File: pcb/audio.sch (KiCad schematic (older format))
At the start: 40 parts, among them J1 AudioJack3_SwitchTR, U400 CS43130, U401 ADP150-3.0, U402 ADP150-1.8, U403 ADP150-1.8, U404 SN74AVC4T245PW, U405 PCA9306, X1 DSC1001CE2-022.5792

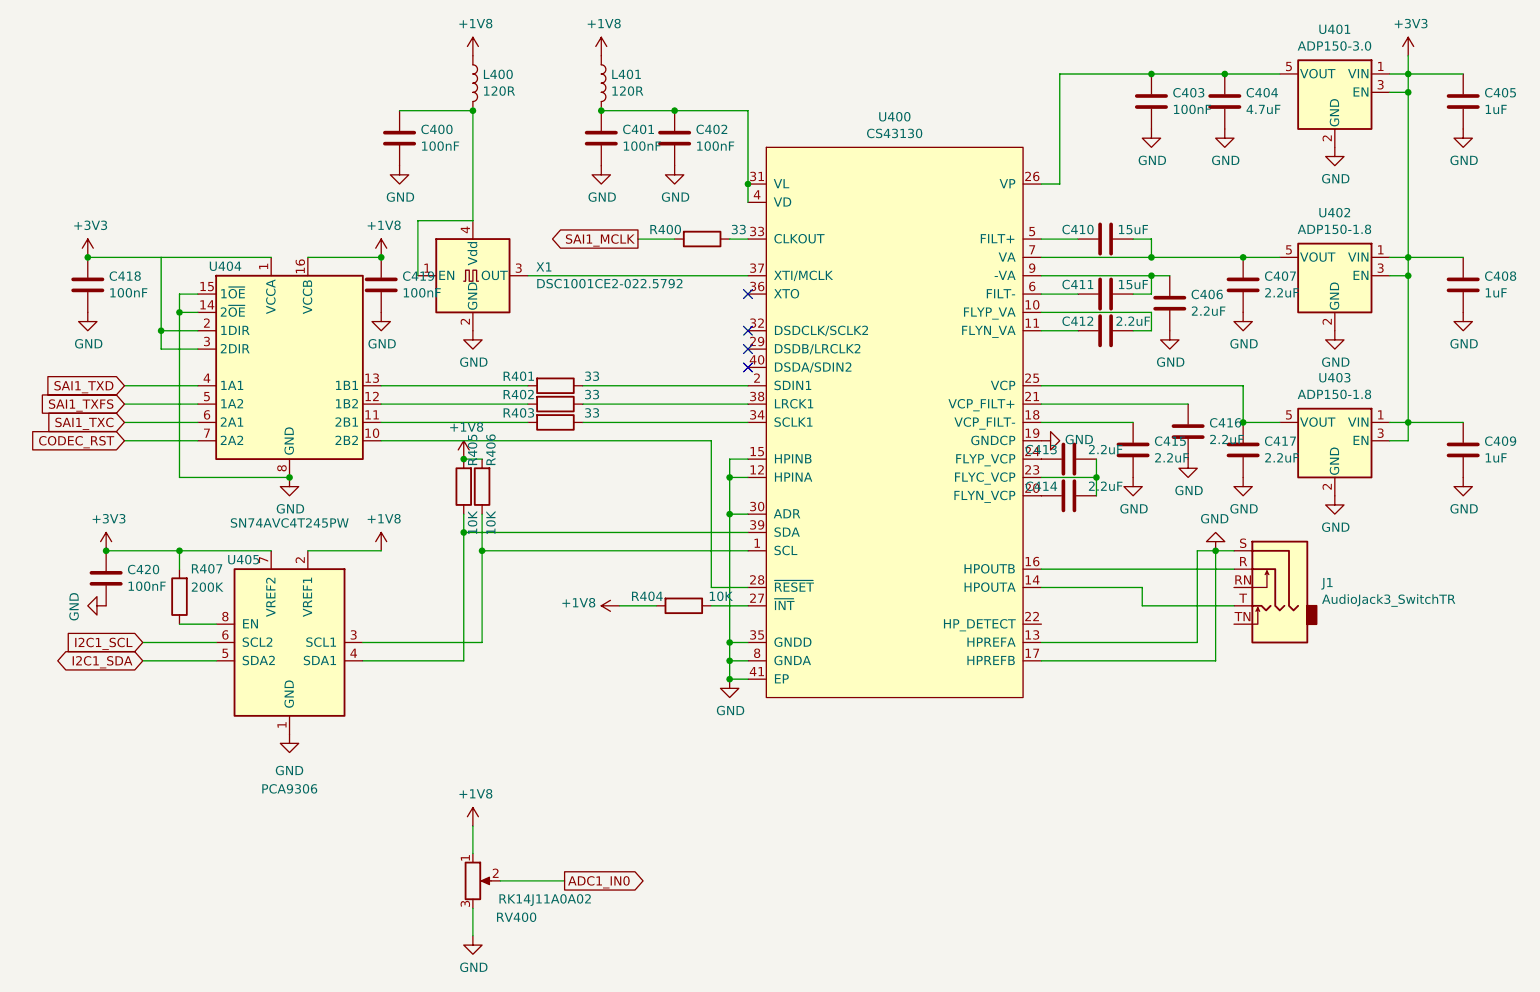
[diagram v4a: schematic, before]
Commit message: pcb: use crystal instead
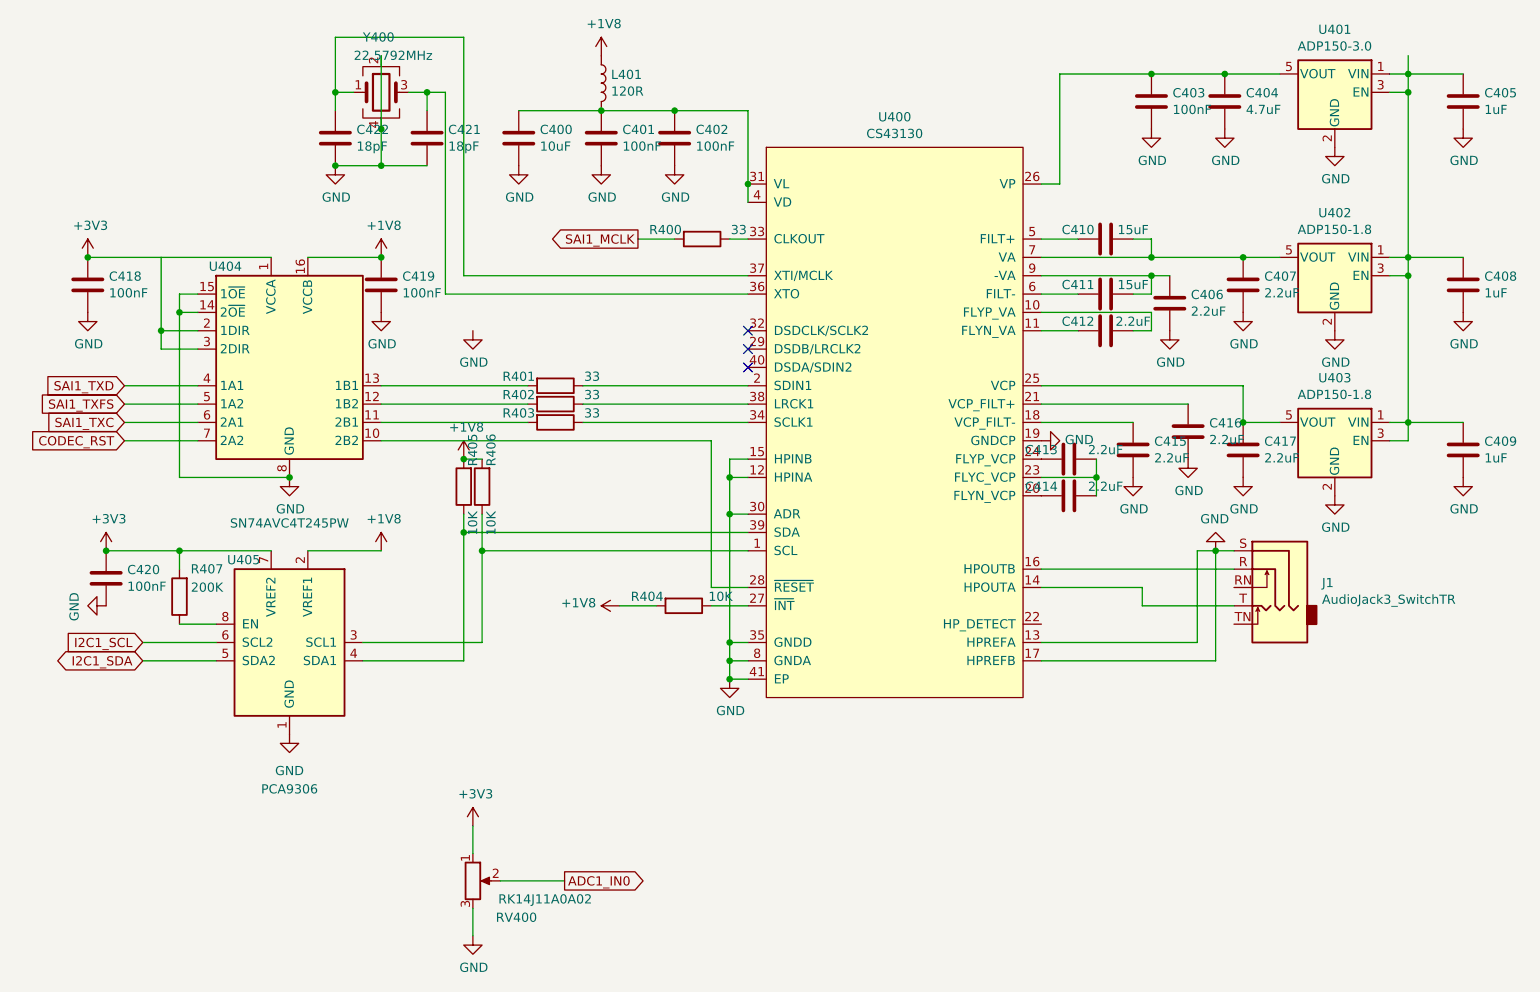
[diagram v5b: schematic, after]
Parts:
- removed L400: 120R, Inductor_SMD:L_0603_1608Metric, symbol Device:L
- removed X1: DSC1001CE2-022.5792, Oscillator:Oscillator_SMD_Abracon_ASE-4Pin_3.2x2.5mm, symbol Oscillator:ASE-xxxMHz
- added C421, C422: 18pF, Capacitor_SMD:C_0402_1005Metric, symbol Device:C
- added Y400: 22.5792MHz, Oscillator:Oscillator_SMD_Abracon_ASE-4Pin_3.2x2.5mm, symbol Device:Crystal_GND24
- C400: value 100nF -> 10uF
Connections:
- net +1V8: no longer RV400.1
- net +3V3: now also RV400.1; no longer C405.1, C408.1, C409.1, U401.1 (VIN), U401.3 (EN), U402.1 (VIN), U402.3 (EN), U403.1 (VIN), U403.3 (EN)
- net GND: now also C421.2, C422.2, Y400.2, Y400.4
- net at C401.1, C402.1, L401.2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: now also C400.1
- net at U400.36 (XTO): now also C421.1, Y400.3
- net at U400.37 (XTI/MCLK): now also C422.1, Y400.1
- new net: C405.1, C408.1, C409.1, U401.1 (VIN), U401.3 (EN), U402.1 (VIN), U402.3 (EN), U403.1 (VIN), U403.3 (EN)
- no-connect marks 4 -> 3
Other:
- moved on the sheet: C400
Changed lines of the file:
@@
 	-1   0    0    -1
-$EndComp
-$Comp
-L power:+3V3 #PWR0252
-U 1 1 5D3C5E19
-P 8600 2300
-F 0 "#PWR0252" H 8600 2150 50  0001 C CNN
-F 1 "+3V3" H 8615 2473 50  0000 C CNN
-F 2 "" H 8600 2300 50  0001 C CNN
-F 3 "" H 8600 2300 50  0001 C CNN
-	1    8600 2300
-	1    0    0    -1
 $EndComp
 Wire Wire Line
@@
 NoConn ~ 5000 3900
 NoConn ~ 5000 4000
-NoConn ~ 5000 3600
-$Comp
-L power:+1V8 #PWR0272
-U 1 1 5D485FE4
-P 3500 2300
-F 0 "#PWR0272" H 3500 2150 50  0001 C CNN
-F 1 "+1V8" H 3515 2473 50  0000 C CNN
-F 2 "" H 3500 2300 50  0001 C CNN
-F 3 "" H 3500 2300 50  0001 C CNN
-	1    3500 2300
-	1    0    0    -1
-$EndComp
 $Comp
 L Device:C C400
 U 1 1 5D487832
-P 3100 2750
-F 0 "C400" H 3215 2796 50  0000 L CNN
-F 1 "100nF" H 3215 2705 50  0000 L CNN
-F 2 "Capacitor_SMD:C_0402_1005Metric" H 3138 2600 50  0001 C CNN
-F 3 "~" H 3100 2750 50  0001 C CNN
-	1    3100 2750
+P 3750 2750
+F 0 "C400" H 3865 2796 50  0000 L CNN
+F 1 "10uF" H 3865 2705 50  0000 L CNN
+F 2 "Capacitor_SMD:C_0402_1005Metric" H 3788 2600 50  0001 C CNN
+F 3 "~" H 3750 2750 50  0001 C CNN
+	1    3750 2750
 	1    0    0    -1
 $EndComp
@@
 L power:GND #PWR0273
 U 1 1 5D487838
-P 3100 2900
-F 0 "#PWR0273" H 3100 2650 50  0001 C CNN
-F 1 "GND" H 3105 2727 50  0000 C CNN
-F 2 "" H 3100 2900 50  0001 C CNN
-F 3 "" H 3100 2900 50  0001 C CNN
-	1    3100 2900
-	1    0    0    -1
-$EndComp
-Wire Wire Line
-	3100 2600 3500 2600
-Wire Wire Line
-	3500 3200 3500 2600
-Connection ~ 3500 2600
+P 3750 2900
+F 0 "#PWR0273" H 3750 2650 50  0001 C CNN
+F 1 "GND" H 3755 2727 50  0000 C CNN
+F 2 "" H 3750 2900 50  0001 C CNN
+F 3 "" H 3750 2900 50  0001 C CNN
+	1    3750 2900
+	1    0    0    -1
+$EndComp
 $Comp
 L power:GND #PWR0274
@@
 	1    0    0    -1
 $EndComp
-Wire Wire Line
-	3200 3500 3200 3200
-Wire Wire Line
-	3200 3200 3500 3200
-Wire Wire Line
-	3800 3500 5000 3500
 $Comp
 L Device:L L401
@@
 F 3 "~" H 4200 2450 50  0001 C CNN
 	1    4200 2450
-	1    0    0    -1
-$EndComp
-$Comp
-L Device:L L400
-U 1 1 5D4999E2
-P 3500 2450
-F 0 "L400" H 3553 2496 50  0000 L CNN
-F 1 "120R" H 3553 2405 50  0000 L CNN
-F 2 "Inductor_SMD:L_0603_1608Metric" H 3500 2450 50  0001 C CNN
-F 3 "~" H 3500 2450 50  0001 C CNN
-	1    3500 2450
 	1    0    0    -1
 $EndComp
@@
 Wire Wire Line
 	1600 4300 2000 4300
-$Comp
-L Oscillator:ASE-xxxMHz X1
-U 1 1 5D80F8A2
-P 3500 3500
-AR Path="/5D438133/5D80F8A2" Ref="X1"  Part="1"
-AR Path="/5DB2122B/5D80F8A2" Ref="X?"  Part="1"
-F 0 "X1" H 3844 3546 50  0000 L CNN
-F 1 "DSC1001CE2-022.5792" H 3844 3455 50  0000 L CNN
-F 2 "Oscillator:Oscillator_SMD_Abracon_ASE-4Pin_3.2x2.5mm" H 4200 3150 50  0001 C CNN
-F 3 "http://www.abracon.com/Oscillators/ASV.pdf" H 3400 3500 50  0001 C CNN
-	1    3500 3500
-	1    0    0    -1
-$EndComp
 Wire Wire Line
 	4100 4100 5000 4100
@@
 	4600 3300 4400 3300
 $Comp
-L power:+1V8 #PWR0102
-U 1 1 5D77A87B
-P 3500 6500
-F 0 "#PWR0102" H 3500 6350 50  0001 C CNN
-F 1 "+1V8" H 3515 6673 50  0000 C CNN
-F 2 "" H 3500 6500 50  0001 C CNN
-F 3 "" H 3500 6500 50  0001 C CNN
-	1    3500 6500
-	1    0    0    -1
-$EndComp
-$Comp
 L Logic_LevelTranslator:SN74AVC4T245PW U404
 U 1 1 5D8C4C20
@@
 Connection ~ 1400 3400
 $Comp
-L power:+1V8 #PWR?
+L power:+1V8 #PWR0142
 U 1 1 5DA41BB7
 P 3000 3400
-F 0 "#PWR?" H 3000 3250 50  0001 C CNN
+F 0 "#PWR0142" H 3000 3250 50  0001 C CNN
 F 1 "+1V8" H 3015 3573 50  0000 C CNN
 F 2 "" H 3000 3400 50  0001 C CNN
@@
 Connection ~ 3000 3400
 $Comp
-L power:GND #PWR?
+L power:GND #PWR0143
 U 1 1 5DA4A9B1
 P 3000 3700
-F 0 "#PWR?" H 3000 3450 50  0001 C CNN
+F 0 "#PWR0143" H 3000 3450 50  0001 C CNN
 F 1 "GND" H 3005 3527 50  0000 C CNN
 F 2 "" H 3000 3700 50  0001 C CNN
@@
 Connection ~ 1500 5000
 $Comp
-L power:GND #PWR?
+L power:GND #PWR0144
 U 1 1 5DA56209
 P 1500 5300
-F 0 "#PWR?" H 1500 5050 50  0001 C CNN
+F 0 "#PWR0144" H 1500 5050 50  0001 C CNN
 F 1 "GND" H 1505 5127 50  0000 C CNN
 F 2 "" H 1500 5300 50  0001 C CNN
@@
 	0    1    1    0
 $EndComp
+$Comp
+L power:+3V3 #PWR?
+U 1 1 5DBD75D1
+P 3500 6500
+F 0 "#PWR?" H 3500 6350 50  0001 C CNN
+F 1 "+3V3" H 3515 6673 50  0000 C CNN
+F 2 "" H 3500 6500 50  0001 C CNN
+F 3 "" H 3500 6500 50  0001 C CNN
+	1    3500 6500
+	1    0    0    -1
+$EndComp
+$Comp
+L Device:Crystal_GND24 Y?
+U 1 1 5DC89C50
+P 3000 2500
+AR Path="/5D4C99F9/5DC89C50" Ref="Y?"  Part="1"
+AR Path="/5D438133/5DC89C50" Ref="Y400"  Part="1"
+F 0 "Y400" H 2900 2800 50  0000 L CNN
+F 1 "22.5792MHz" H 2850 2700 50  0000 L CNN
+F 2 "Oscillator:Oscillator_SMD_Abracon_ASE-4Pin_3.2x2.5mm" H 3000 2500 50  0001 C CNN
+F 3 "~" H 3000 2500 50  0001 C CNN
+	1    3000 2500
+	1    0    0    -1
+$EndComp
+$Comp
+L Device:C C?
+U 1 1 5DC89C56
+P 2750 2750
+AR Path="/5D4C99F9/5DC89C56" Ref="C?"  Part="1"
+AR Path="/5D438133/5DC89C56" Ref="C422"  Part="1"
+F 0 "C422" H 2865 2796 50  0000 L CNN
+F 1 "18pF" H 2865 2705 50  0000 L CNN
+F 2 "Capacitor_SMD:C_0402_1005Metric" H 2788 2600 50  0001 C CNN
+F 3 "~" H 2750 2750 50  0001 C CNN
+	1    2750 2750
+	1    0    0    -1
+$EndComp
+$Comp
+L Device:C C?
+U 1 1 5DC89C5C
+P 3250 2750
+AR Path="/5D4C99F9/5DC89C5C" Ref="C?"  Part="1"
+AR Path="/5D438133/5DC89C5C" Ref="C421"  Part="1"
+F 0 "C421" H 3365 2796 50  0000 L CNN
+F 1 "18pF" H 3365 2705 50  0000 L CNN
+F 2 "Capacitor_SMD:C_0402_1005Metric" H 3288 2600 50  0001 C CNN
+F 3 "~" H 3250 2750 50  0001 C CNN
+	1    3250 2750
+	1    0    0    -1
+$EndComp
+$Comp
+L power:GND #PWR?
+U 1 1 5DC89C62
+P 2750 2900
+AR Path="/5D4C99F9/5DC89C62" Ref="#PWR?"  Part="1"
+AR Path="/5D438133/5DC89C62" Ref="#PWR?"  Part="1"
+F 0 "#PWR?" H 2750 2650 50  0001 C CNN
+F 1 "GND" H 2755 2727 50  0000 C CNN
+F 2 "" H 2750 2900 50  0001 C CNN
+F 3 "" H 2750 2900 50  0001 C CNN
+	1    2750 2900
+	1    0    0    -1
+$EndComp
+Wire Wire Line
+	2750 2600 2750 2500
+Wire Wire Line
+	2850 2500 2750 2500
+Connection ~ 2750 2500
+Wire Wire Line
+	2750 2500 2750 2200
+Wire Wire Line
+	3150 2500 3250 2500
+Wire Wire Line
+	3250 2500 3250 2600
+Wire Wire Line
+	3250 2900 3000 2900
+Connection ~ 2750 2900
+Connection ~ 3000 2900
+Wire Wire Line
+	3000 2900 2750 2900
+Wire Wire Line
+	3000 2300 3000 2700
+Connection ~ 3000 2700
+Wire Wire Line
+	3000 2700 3000 2900
+Wire Wire Line
+	3750 2600 4200 2600
+Wire Wire Line
+	3250 2500 3350 2500
+Wire Wire Line
+	3350 2500 3350 3600
+Wire Wire Line
+	3350 3600 5000 3600
+Connection ~ 3250 2500
+Wire Wire Line
+	5000 3500 3450 3500
+Wire Wire Line
+	3450 3500 3450 2200
+Wire Wire Line
+	3450 2200 2750 2200
 $EndSCHEMATC
